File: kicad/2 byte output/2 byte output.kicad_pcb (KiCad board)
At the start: 2 copper layers, 88.9 x 53.3 mm, 12 parts, among them J1 Conn_01x05_Male, J2 Conn_01x05_Female, J3 Screw_Terminal_01x16, J4 Screw_Terminal_01x02, U1 74HCT595, U2 ULN2803A, U3 74HCT595, U4 ULN2803A

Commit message: periodic check in
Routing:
- net GND: track 0.00 -> 273.1 mm, vias 0 -> 7
- net VCC: track 40.1 -> 157.5 mm
- net OUT9: track 12.6 -> 17.8 mm
- net OUT1: track 12.6 -> 17.8 mm
- net OUT15: track 11.5 -> 15.2 mm
- net OUT2: track 11.5 -> 15.2 mm
- net OUT7: track 11.5 -> 15.2 mm
- net OUT10: track 11.5 -> 15.2 mm
- net OUT8: track 14.8 -> 17.8 mm
- net OUT16: track 15.2 -> 17.8 mm
- net OUT14: track 10.5 -> 12.7 mm
- net OUT11: track 10.5 -> 12.7 mm
- net OUT3: track 10.5 -> 12.7 mm
- net OUT6: track 10.5 -> 12.7 mm
- net COM: track 55.3 -> 57.1 mm
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- removed copper zone on B.Cu, net GND
- removed copper zone on F.Cu, net VCC

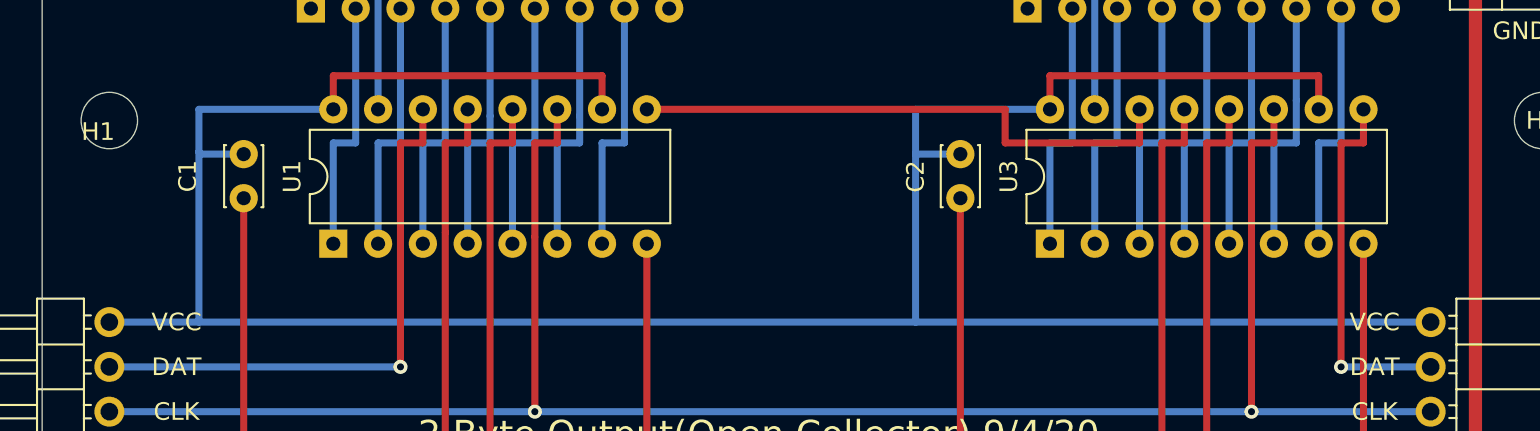
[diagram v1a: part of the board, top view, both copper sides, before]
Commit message: rerouted several PCBs
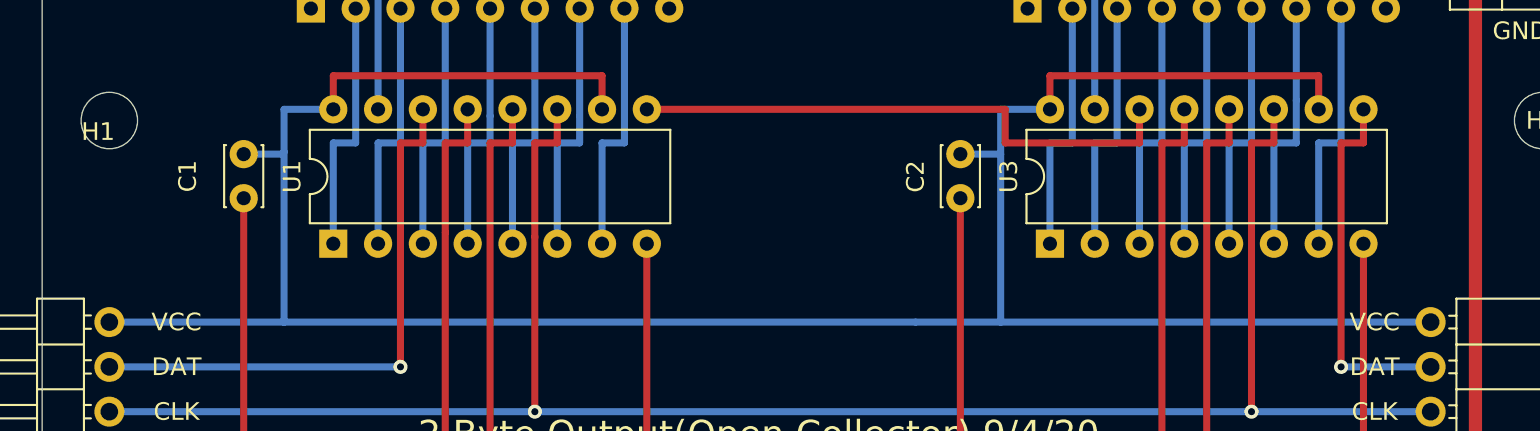
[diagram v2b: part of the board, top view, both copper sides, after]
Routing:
- net VCC: track 157.5 -> 147.4 mm

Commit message: added dcc sniffer, conversion to kicad 6
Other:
- net class Default removed
- net class power removed
